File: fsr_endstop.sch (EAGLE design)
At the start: 32 parts, among them U1 ATTINY461

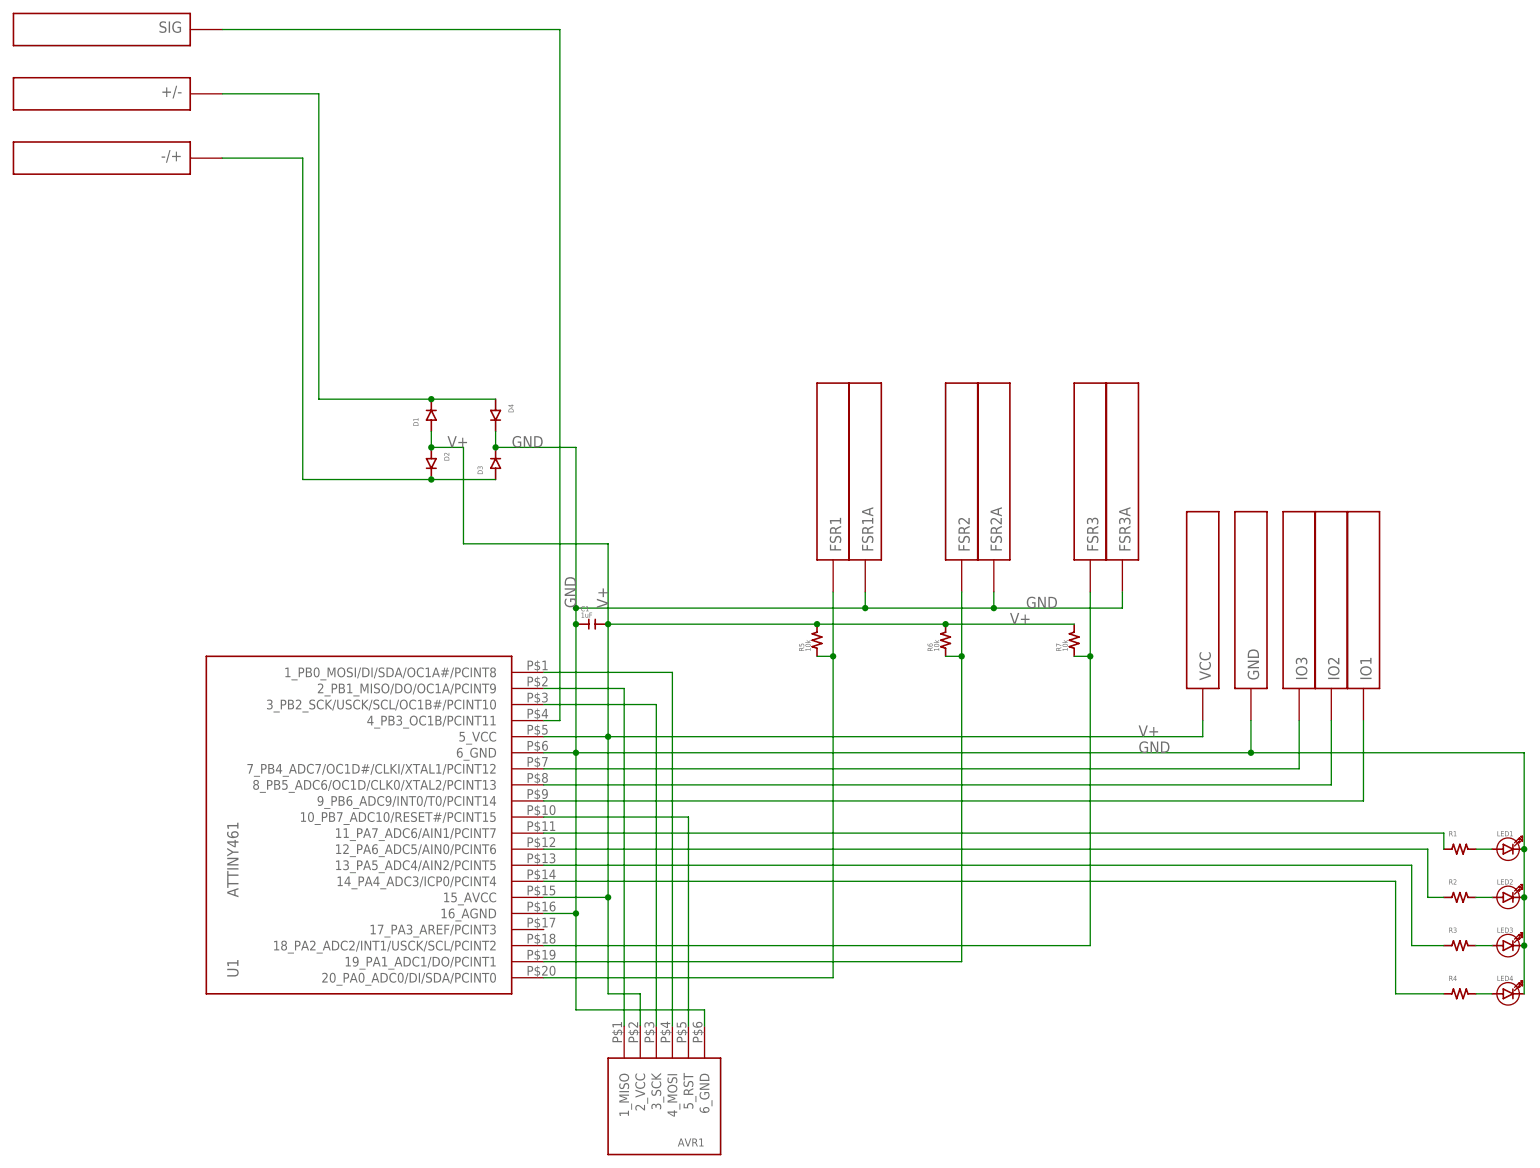
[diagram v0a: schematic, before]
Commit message: Completed routing
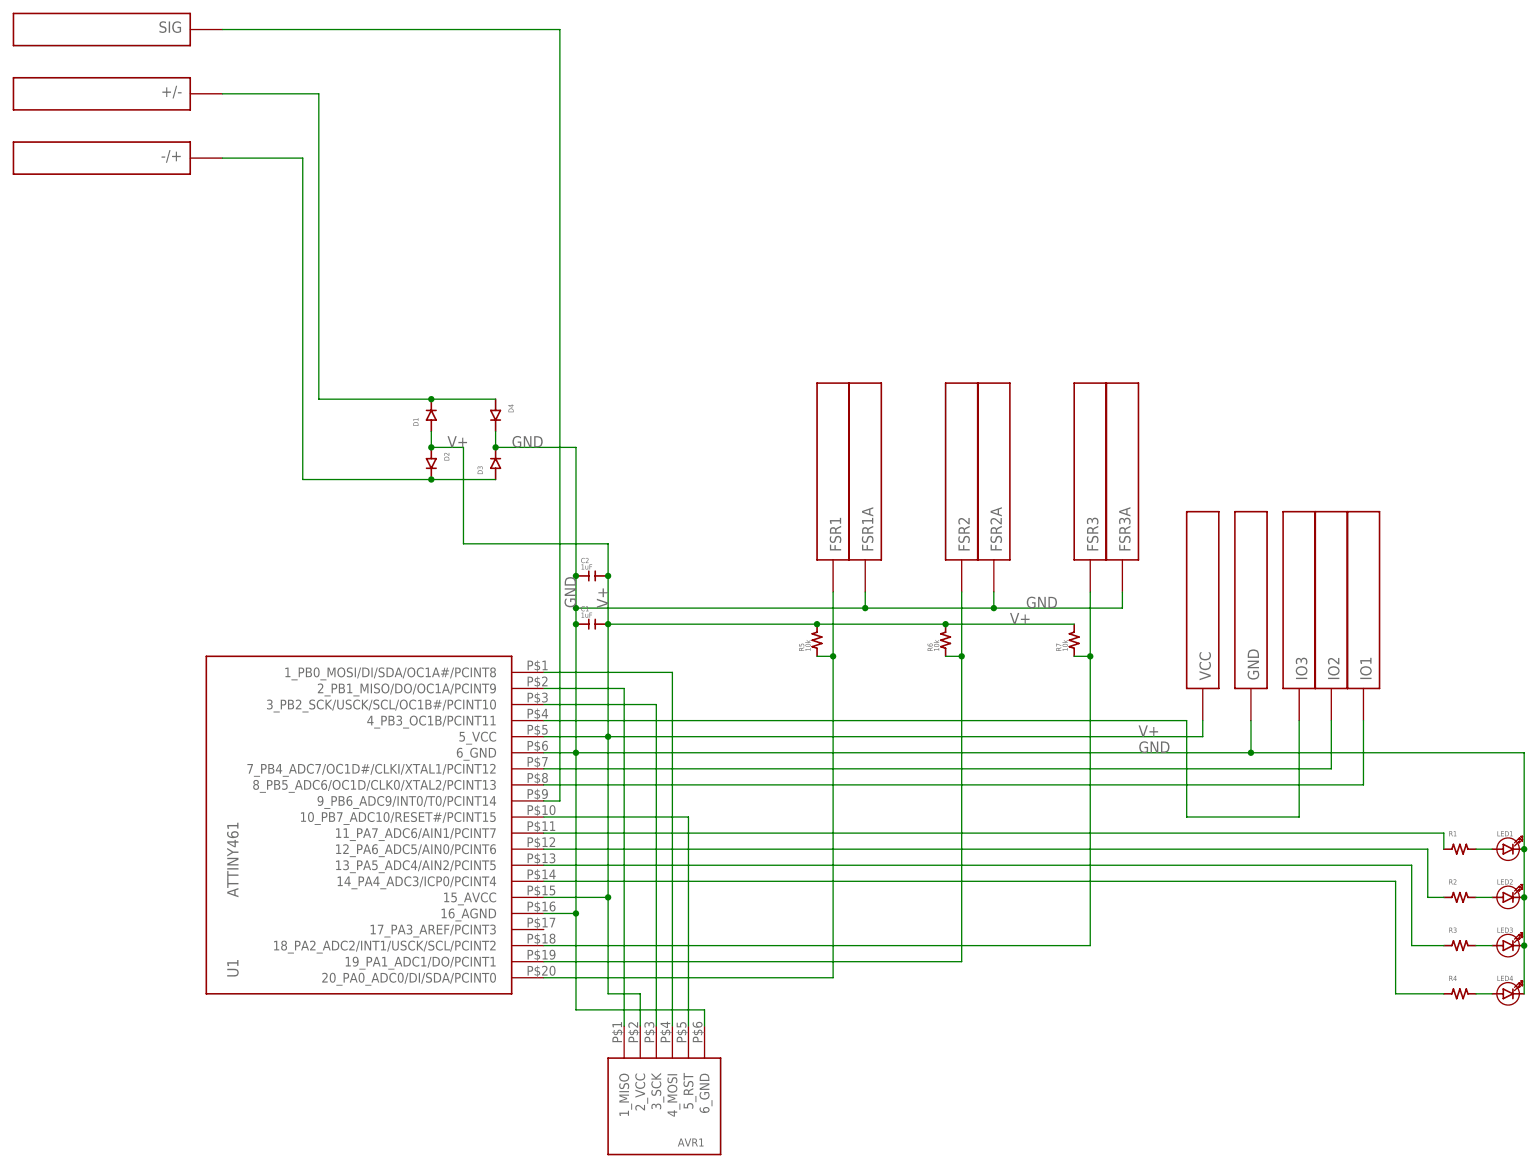
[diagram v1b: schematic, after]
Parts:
- added C2: 1uF, _sg_lib:CAP0603
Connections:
- net GND: now also C2.P$1
- net N$14: now also U1.9_PB6_ADC9/INT0/T0/PCINT14; no longer U1.4_PB3_OC1B/PCINT11
- net N$15: now also IO3.P$1, U1.4_PB3_OC1B/PCINT11; no longer IO1.P$1, U1.9_PB6_ADC9/INT0/T0/PCINT14
- net N$16: now also IO1.P$1; no longer IO2.P$1
- net N$17: now also IO2.P$1; no longer IO3.P$1
- net V+: now also C2.P$2
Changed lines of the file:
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@@
 <part name="GND" library="_sg_lib" deviceset="PIN" device="1.2MM"/>
 <part name="VCC" library="_sg_lib" deviceset="PIN" device="1.2MM"/>
+<part name="C2" library="_sg_lib" deviceset="CAP0603" device="" value="1uF"/>
 </parts>
 <sheets>
@@
 <instance part="GND" gate="G$1" x="149.86" y="68.58" rot="R270"/>
 <instance part="VCC" gate="G$1" x="142.24" y="68.58" rot="R270"/>
+<instance part="C2" gate="G$1" x="45.72" y="86.36"/>
 </instances>
 <busses>
@@
 <junction x="48.26" y="60.96"/>
 <wire x1="25.4" y1="91.44" x2="48.26" y2="91.44" width="0.1524" layer="91"/>
-<wire x1="48.26" y1="91.44" x2="48.26" y2="78.74" width="0.1524" layer="91"/>
+<wire x1="48.26" y1="91.44" x2="48.26" y2="86.36" width="0.1524" layer="91"/>
 <junction x="48.26" y="78.74"/>
 <label x="48.26" y="81.28" size="1.778" layer="95" rot="R90"/>
 <label x="22.86" y="106.68" size="1.778" layer="95"/>
+<wire x1="48.26" y1="86.36" x2="48.26" y2="78.74" width="0.1524" layer="91"/>
 <wire x1="48.26" y1="35.56" x2="48.26" y2="20.32" width="0.1524" layer="91"/>
 <junction x="48.26" y="35.56"/>
@@
 <wire x1="142.24" y1="60.96" x2="142.24" y2="63.5" width="0.1524" layer="91"/>
 <label x="132.08" y="60.96" size="1.778" layer="95"/>
+<pinref part="C2" gate="G$1" pin="P$2"/>
+<junction x="48.26" y="86.36"/>
 </segment>
 </net>
@@
 <junction x="43.18" y="58.42"/>
 <wire x1="30.48" y1="106.68" x2="43.18" y2="106.68" width="0.1524" layer="91"/>
-<wire x1="43.18" y1="106.68" x2="43.18" y2="81.28" width="0.1524" layer="91"/>
+<wire x1="43.18" y1="106.68" x2="43.18" y2="86.36" width="0.1524" layer="91"/>
 <junction x="30.48" y="106.68"/>
 <junction x="43.18" y="78.74"/>
 <label x="43.18" y="81.28" size="1.778" layer="95" rot="R90"/>
 <label x="33.02" y="106.68" size="1.778" layer="95"/>
+<wire x1="43.18" y1="86.36" x2="43.18" y2="81.28" width="0.1524" layer="91"/>
 <wire x1="43.18" y1="81.28" x2="43.18" y2="78.74" width="0.1524" layer="91"/>
 <wire x1="43.18" y1="33.02" x2="43.18" y2="17.78" width="0.1524" layer="91"/>
@@
 <junction x="193.04" y="27.94"/>
 <pinref part="LED4" gate="G$1" pin="-"/>
+<pinref part="C2" gate="G$1" pin="P$1"/>
+<junction x="43.18" y="86.36"/>
 </segment>
 </net>
@@
 <net name="N$14" class="0">
 <segment>
-<pinref part="U1" gate="G$1" pin="4_PB3_OC1B/PCINT11"/>
-<wire x1="38.1" y1="63.5" x2="40.64" y2="63.5" width="0.1524" layer="91"/>
-<wire x1="40.64" y1="63.5" x2="40.64" y2="172.72" width="0.1524" layer="91"/>
+<wire x1="40.64" y1="50.8" x2="40.64" y2="172.72" width="0.1524" layer="91"/>
 <pinref part="SIG" gate="G$1" pin="P$1"/>
 <wire x1="-12.7" y1="172.72" x2="40.64" y2="172.72" width="0.1524" layer="91"/>
-</segment>
-</net>
-<net name="N$15" class="0">
-<segment>
 <pinref part="U1" gate="G$1" pin="9_PB6_ADC9/INT0/T0/PCINT14"/>
-<wire x1="38.1" y1="50.8" x2="167.64" y2="50.8" width="0.1524" layer="91"/>
+<wire x1="38.1" y1="50.8" x2="40.64" y2="50.8" width="0.1524" layer="91"/>
+</segment>
+</net>
+<net name="N$16" class="0">
+<segment>
+<pinref part="U1" gate="G$1" pin="8_PB5_ADC6/OC1D/CLK0/XTAL2/PCINT13"/>
+<wire x1="38.1" y1="53.34" x2="167.64" y2="53.34" width="0.1524" layer="91"/>
 <pinref part="IO1" gate="G$1" pin="P$1"/>
-<wire x1="167.64" y1="50.8" x2="167.64" y2="63.5" width="0.1524" layer="91"/>
-</segment>
-</net>
-<net name="N$16" class="0">
-<segment>
-<pinref part="U1" gate="G$1" pin="8_PB5_ADC6/OC1D/CLK0/XTAL2/PCINT13"/>
+<wire x1="167.64" y1="53.34" x2="167.64" y2="63.5" width="0.1524" layer="91"/>
+</segment>
+</net>
+<net name="N$17" class="0">
+<segment>
+<pinref part="U1" gate="G$1" pin="7_PB4_ADC7/OC1D#/CLKI/XTAL1/PCINT12"/>
+<wire x1="38.1" y1="55.88" x2="162.56" y2="55.88" width="0.1524" layer="91"/>
 <pinref part="IO2" gate="G$1" pin="P$1"/>
-<wire x1="38.1" y1="53.34" x2="162.56" y2="53.34" width="0.1524" layer="91"/>
-<wire x1="162.56" y1="53.34" x2="162.56" y2="63.5" width="0.1524" layer="91"/>
-</segment>
-</net>
-<net name="N$17" class="0">
-<segment>
-<pinref part="U1" gate="G$1" pin="7_PB4_ADC7/OC1D#/CLKI/XTAL1/PCINT12"/>
-<pinref part="IO3" gate="G$1" pin="P$1"/>
-<wire x1="38.1" y1="55.88" x2="157.48" y2="55.88" width="0.1524" layer="91"/>
-<wire x1="157.48" y1="55.88" x2="157.48" y2="63.5" width="0.1524" layer="91"/>
+<wire x1="162.56" y1="55.88" x2="162.56" y2="63.5" width="0.1524" layer="91"/>
 </segment>
 </net>
@@
 </segment>
 </net>
+<net name="N$15" class="0">
+<segment>
+<pinref part="U1" gate="G$1" pin="4_PB3_OC1B/PCINT11"/>
+<wire x1="38.1" y1="63.5" x2="139.7" y2="63.5" width="0.1524" layer="91"/>
+<wire x1="139.7" y1="63.5" x2="139.7" y2="48.26" width="0.1524" layer="91"/>
+<pinref part="IO3" gate="G$1" pin="P$1"/>
+<wire x1="139.7" y1="48.26" x2="157.48" y2="48.26" width="0.1524" layer="91"/>
+<wire x1="157.48" y1="48.26" x2="157.48" y2="63.5" width="0.1524" layer="91"/>
+</segment>
+</net>
